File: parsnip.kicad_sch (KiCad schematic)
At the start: 68 parts, among them J1 SPI BUS, J2 I2C3, J3 I2C1, J4 I2C2, J5 e-Ink Display Connector, J6 UART0, SW1 ESP_RESET, SW2 BOOT, U1 ESP32-S3-WROOM-1-N16R8, Y1 32.768KHz

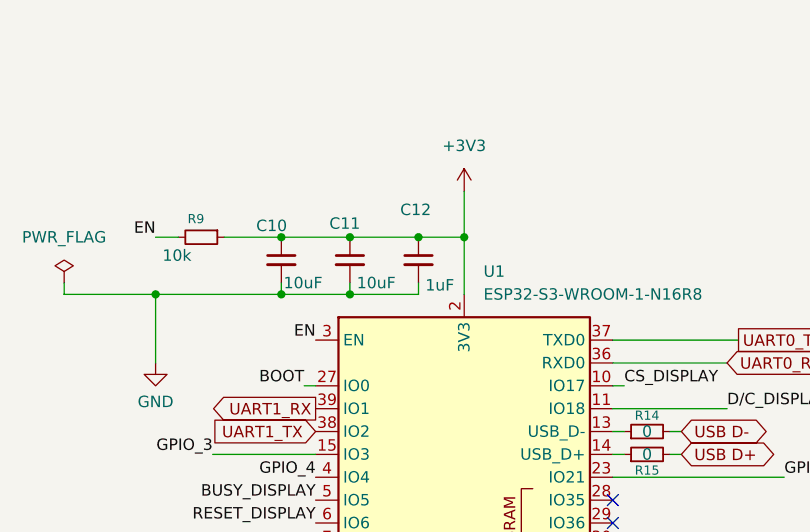
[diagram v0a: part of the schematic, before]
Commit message: change capacitor sizing & update footprints
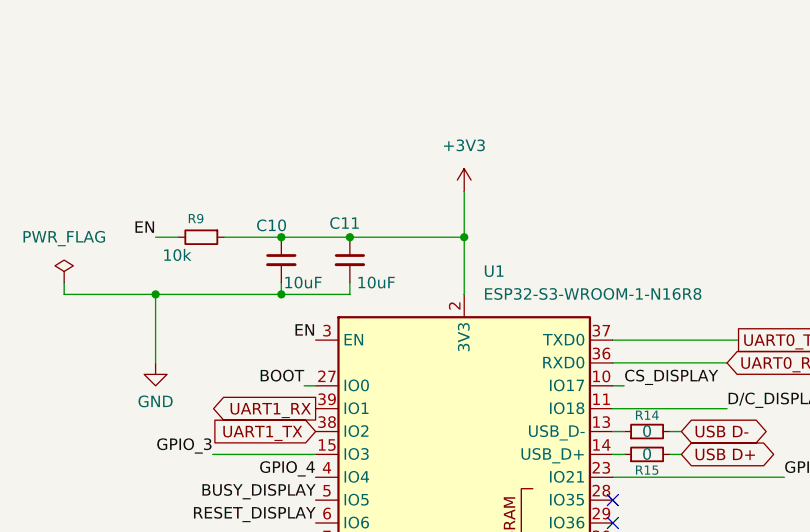
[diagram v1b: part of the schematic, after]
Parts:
- removed C12: 1uF, Capacitor_SMD:C_0402_1005Metric, symbol Device:C_Small
- SW1, SW2: LCSC Part C2681476 -> C202388
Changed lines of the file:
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@@
 	)
 	(junction
-		(at 83.82 36.83)
-		(diameter 0)
-		(color 0 0 0 0)
-	)
-	(junction
 		(at 30.48 170.18)
 		(diameter 0)
@@
 	)
 	(junction
-		(at 76.2 43.18)
-		(diameter 0)
-		(color 0 0 0 0)
-	)
-	(junction
 		(at 269.24 121.92)
 		(diameter 0)
@@
 	(wire
 		(pts
-			(xy 76.2 36.83) (xy 83.82 36.83)
+			(xy 76.2 36.83) (xy 88.9 36.83)
 		)
 		(stroke
@@
 	(wire
 		(pts
-			(xy 76.2 43.18) (xy 83.82 43.18)
-		)
-		(stroke
-			(width 0)
-			(type default)
-		)
-	)
-	(wire
-		(pts
 			(xy 236.22 49.53) (xy 248.92 49.53)
 		)
@@
 	(wire
 		(pts
-			(xy 83.82 43.18) (xy 83.82 41.91)
-		)
-		(stroke
-			(width 0)
-			(type default)
-		)
-	)
-	(wire
-		(pts
 			(xy 30.48 170.18) (xy 30.48 173.99)
 		)
@@
 	(wire
 		(pts
-			(xy 83.82 36.83) (xy 88.9 36.83)
-		)
-		(stroke
-			(width 0)
-			(type default)
-		)
-	)
-	(wire
-		(pts
 			(xy 251.46 127) (xy 256.54 127)
 		)
@@
 			)
 		)
-		(property "LCSC Part" "C2681476"
+		(property "LCSC Part" "C202388"
 			(at 177.8 29.21 0)
 			(hide yes)
@@
 	)
 	(symbol
-		(lib_id "Device:C_Small")
-		(at 83.82 39.37 0)
-		(unit 1)
-		(body_style 1)
-		(exclude_from_sim no)
-		(in_bom yes)
-		(on_board yes)
-		(in_pos_files yes)
-		(dnp no)
-		(property "Reference" "C12"
-			(at 81.788 33.782 0)
-			(show_name no)
-			(do_not_autoplace no)
-			(effects
-				(font
-					(size 1.27 1.27)
-				)
-				(justify left)
-			)
-		)
-		(property "Value" "1uF"
-			(at 84.582 42.164 0)
-			(show_name no)
-			(do_not_autoplace no)
-			(effects
-				(font
-					(size 1.27 1.27)
-				)
-				(justify left)
-			)
-		)
-		(property "Footprint" "Capacitor_SMD:C_0402_1005Metric"
-			(at 83.82 39.37 0)
-			(hide yes)
-			(show_name no)
-			(do_not_autoplace no)
-			(effects
-				(font
-					(size 1.27 1.27)
-				)
-			)
-		)
-		(property "Datasheet" ""
-			(at 83.82 39.37 0)
-			(hide yes)
-			(show_name no)
-			(do_not_autoplace no)
-			(effects
-				(font
-					(size 1.27 1.27)
-				)
-			)
-		)
-		(property "Description" "Unpolarized capacitor, small symbol"
-			(at 83.82 39.37 0)
-			(hide yes)
-			(show_name no)
-			(do_not_autoplace no)
-			(effects
-				(font
-					(size 1.27 1.27)
-				)
-			)
-		)
-		(property "LCSC Part" "C53426846"
-			(at 83.82 39.37 0)
-			(hide yes)
-			(show_name no)
-			(do_not_autoplace no)
-			(effects
-				(font
-					(size 1.27 1.27)
-				)
-			)
-		)
-		(property "Voltage Rating" "25V"
-			(at 81.026 38.862 0)
-			(hide yes)
-			(show_name no)
-			(do_not_autoplace no)
-			(effects
-				(font
-					(size 1.27 1.27)
-				)
-			)
-		)
-		(property "Tolerance" ""
-			(at 83.82 39.37 0)
-			(hide yes)
-			(show_name no)
-			(do_not_autoplace no)
-			(effects
-				(font
-					(size 1.27 1.27)
-				)
-			)
-		)
-		(property "LCSC" ""
-			(at 83.82 39.37 0)
-			(hide yes)
-			(show_name no)
-			(do_not_autoplace no)
-			(effects
-				(font
-					(size 1.27 1.27)
-				)
-			)
-		)
-		(property "KLC_S3.3" ""
-			(at 83.82 39.37 0)
-			(hide yes)
-			(show_name no)
-			(do_not_autoplace no)
-			(effects
-				(font
-					(size 1.27 1.27)
-				)
-			)
-		)
-		(property "KLC_S5.1" ""
-			(at 83.82 39.37 0)
-			(hide yes)
-			(show_name no)
-			(do_not_autoplace no)
-			(effects
-				(font
-					(size 1.27 1.27)
-				)
-			)
-		)
-		(property "Capacitor Rating" "X7R"
-			(at 83.82 39.37 0)
-			(hide yes)
-			(show_name no)
-			(do_not_autoplace no)
-			(effects
-				(font
-					(size 1.27 1.27)
-				)
-			)
-		)
-		(pin "2"
-		)
-		(pin "1"
-		)
-		(instances
-			(project "parsnip"
-				(path "/fe9d4a31-2311-442f-997c-52ad8ca5cfe9"
-					(reference "C12")
-					(unit 1)
-				)
-			)
-		)
-	)
-	(symbol
 		(lib_id "Device:R_Small")
 		(at 259.08 142.24 90)
@@
 			)
 		)
-		(property "LCSC Part" "C2681476"
+		(property "LCSC Part" "C202388"
 			(at 139.7 29.21 0)
 			(hide yes)

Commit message: assign lcsc part numbers
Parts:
- J4: now left out of the parts list
- J6: LCSC Part (none) -> C160403
- R20, R24, R25, R26, R7, R9: LCSC Part C2902636 -> C54951138
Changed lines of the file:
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@@
 		(body_style 1)
 		(exclude_from_sim no)
-		(in_bom yes)
+		(in_bom no)
 		(on_board yes)
 		(in_pos_files yes)
@@
 			)
 		)
+		(property "Capacitor Rating" ""
+			(at 113.03 177.8 0)
+			(hide yes)
+			(show_name no)
+			(do_not_autoplace no)
+			(effects
+				(font
+					(size 1.27 1.27)
+				)
+			)
+		)
 		(pin "2"
 		)
@@
 			)
 		)
-		(property "LCSC Part" "C2902636"
+		(property "LCSC Part" "C54951138"
 			(at 59.69 36.83 0)
 			(hide yes)
@@
 			)
 		)
-		(property "LCSC Part" "C2902636"
+		(property "LCSC Part" "C54951138"
 			(at 259.08 153.67 0)
 			(hide yes)
@@
 			)
 		)
-		(property "LCSC Part" "C2902636"
+		(property "LCSC Part" "C54951138"
 			(at 154.94 21.59 0)
 			(hide yes)
@@
 			)
 		)
-		(property "LCSC Part" "C2902636"
+		(property "LCSC Part" "C54951138"
 			(at 259.08 147.32 0)
 			(hide yes)
@@
 			)
 		)
-		(property "LCSC Part" "C2902636"
+		(property "LCSC Part" "C54951138"
 			(at 248.92 121.92 0)
 			(hide yes)
@@
 			)
 		)
-		(property "LCSC Part" "C2902636"
+		(property "LCSC Part" "C54951138"
 			(at 259.08 142.24 0)
 			(hide yes)
@@
 			)
 		)
-		(property "LCSC Part" ""
+		(property "LCSC Part" "C160403"
 			(at 198.12 147.32 0)
 			(hide yes)

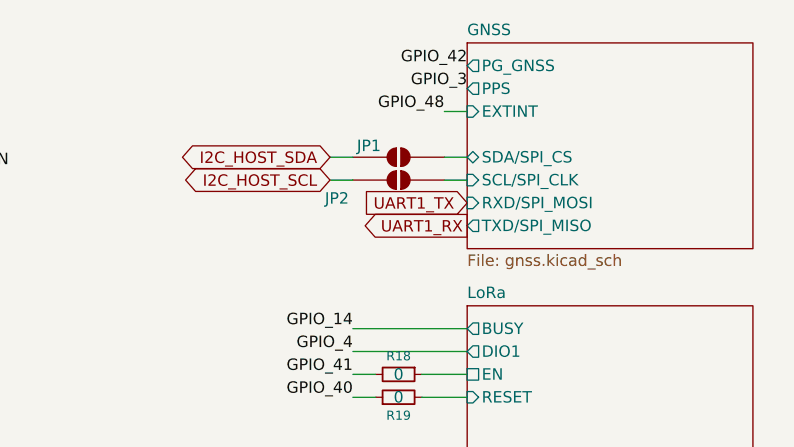
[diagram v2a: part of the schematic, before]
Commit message: Update GNSS schematic to work with NEO-F10N by changing symbol & replacing SAW filter
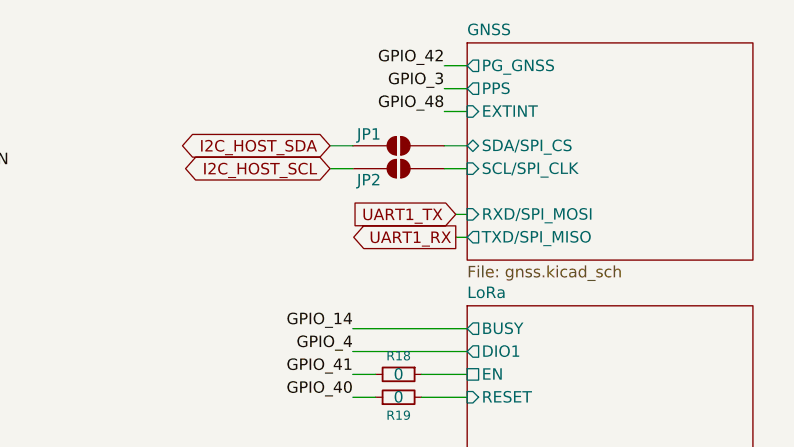
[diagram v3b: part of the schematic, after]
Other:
- moved on the sheet: JP1, JP2
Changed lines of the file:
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@@
 	(wire
 		(pts
+			(xy 246.38 17.78) (xy 248.92 17.78)
+		)
+		(stroke
+			(width 0)
+			(type default)
+		)
+	)
+	(wire
+		(pts
 			(xy 180.34 34.29) (xy 185.42 34.29)
 		)
@@
 	(wire
 		(pts
+			(xy 233.68 26.67) (xy 236.22 26.67)
+		)
+		(stroke
+			(width 0)
+			(type default)
+		)
+	)
+	(wire
+		(pts
 			(xy 62.23 104.14) (xy 62.23 97.79)
 		)
@@
 	(wire
 		(pts
-			(xy 233.68 27.94) (xy 236.22 27.94)
+			(xy 246.38 26.67) (xy 248.92 26.67)
 		)
 		(stroke
@@
 	(wire
 		(pts
+			(xy 246.38 20.32) (xy 248.92 20.32)
+		)
+		(stroke
+			(width 0)
+			(type default)
+		)
+	)
+	(wire
+		(pts
 			(xy 111.76 60.96) (xy 113.03 60.96)
 		)
@@
 	(wire
 		(pts
+			(xy 233.68 29.21) (xy 236.22 29.21)
+		)
+		(stroke
+			(width 0)
+			(type default)
+		)
+	)
+	(wire
+		(pts
 			(xy 44.45 43.18) (xy 54.61 43.18)
 		)
@@
 	(wire
 		(pts
-			(xy 22.86 170.18) (xy 30.48 170.18)
+			(xy 246.38 29.21) (xy 248.92 29.21)
 		)
 		(stroke
@@
 	(wire
 		(pts
-			(xy 142.24 176.53) (xy 138.43 176.53)
+			(xy 247.65 34.29) (xy 248.92 34.29)
 		)
 		(stroke
@@
 	(wire
 		(pts
-			(xy 246.38 27.94) (xy 248.92 27.94)
+			(xy 22.86 170.18) (xy 30.48 170.18)
+		)
+		(stroke
+			(width 0)
+			(type default)
+		)
+	)
+	(wire
+		(pts
+			(xy 142.24 176.53) (xy 138.43 176.53)
 		)
 		(stroke
@@
 	(wire
 		(pts
-			(xy 124.46 63.5) (xy 105.41 63.5)
+			(xy 247.65 36.83) (xy 248.92 36.83)
 		)
 		(stroke
@@
 	(wire
 		(pts
-			(xy 269.24 127) (xy 269.24 132.08)
+			(xy 124.46 63.5) (xy 105.41 63.5)
 		)
 		(stroke
@@
 	(wire
 		(pts
-			(xy 88.9 31.75) (xy 88.9 36.83)
+			(xy 269.24 127) (xy 269.24 132.08)
 		)
 		(stroke
@@
 	(wire
 		(pts
-			(xy 246.38 30.48) (xy 248.92 30.48)
+			(xy 88.9 31.75) (xy 88.9 36.83)
 		)
 		(stroke
@@
 	(wire
 		(pts
-			(xy 233.68 30.48) (xy 236.22 30.48)
-		)
-		(stroke
-			(width 0)
-			(type default)
-		)
-	)
-	(wire
-		(pts
 			(xy 146.05 29.21) (xy 147.32 29.21)
 		)
@@
 	)
 	(label "GPIO_42"
-		(at 248.92 17.78 180)
+		(at 246.38 17.78 180)
 		(effects
 			(font
@@
 	)
 	(label "GPIO_3"
-		(at 248.92 20.32 180)
+		(at 246.38 20.32 180)
 		(effects
 			(font
@@
 	(global_label "UART1_RX"
 		(shape output)
-		(at 248.92 35.56 180)
+		(at 247.65 36.83 180)
 		(fields_autoplaced yes)
 		(effects
@@
 		)
 		(property "Intersheetrefs" "${INTERSHEET_REFS}"
-			(at 236.6215 35.56 0)
+			(at 235.3515 36.83 0)
 			(hide yes)
 			(show_name no)
@@
 	(global_label "I2C_HOST_SCL"
 		(shape bidirectional)
-		(at 233.68 30.48 180)
+		(at 233.68 29.21 180)
 		(fields_autoplaced yes)
 		(effects
@@
 		)
 		(property "Intersheetrefs" "${INTERSHEET_REFS}"
-			(at 216.2183 30.48 0)
+			(at 216.2183 29.21 0)
 			(hide yes)
 			(show_name no)
@@
 	(global_label "I2C_HOST_SDA"
 		(shape bidirectional)
-		(at 233.68 27.94 180)
+		(at 233.68 26.67 180)
 		(fields_autoplaced yes)
 		(effects
@@
 		)
 		(property "Intersheetrefs" "${INTERSHEET_REFS}"
-			(at 216.1578 27.94 0)
+			(at 216.1578 26.67 0)
 			(hide yes)
 			(show_name no)
@@
 	(global_label "UART1_TX"
 		(shape input)
-		(at 248.92 33.02 180)
+		(at 247.65 34.29 180)
 		(fields_autoplaced yes)
 		(effects
@@
 		)
 		(property "Intersheetrefs" "${INTERSHEET_REFS}"
-			(at 236.9239 33.02 0)
+			(at 235.6539 34.29 0)
 			(hide yes)
 			(show_name no)
@@
 	(symbol
 		(lib_id "Jumper:SolderJumper_2_Open")
-		(at 241.3 30.48 0)
+		(at 241.3 29.21 0)
 		(unit 1)
 		(body_style 1)
@@
 		(dnp no)
 		(property "Reference" "JP2"
-			(at 234.442 32.512 0)
+			(at 237.998 30.48 0)
 			(show_name no)
 			(do_not_autoplace no)
@@
 		)
 		(property "Value" "SolderJumper_2_Open"
-			(at 241.3 26.67 0)
+			(at 241.3 25.4 0)
 			(hide yes)
 			(show_name no)
@@
 		)
 		(property "Footprint" "Jumper:SolderJumper-2_P1.3mm_Open_TrianglePad1.0x1.5mm"
-			(at 241.3 30.48 0)
+			(at 241.3 29.21 0)
 			(hide yes)
 			(show_name no)
@@
 		)
 		(property "Datasheet" ""
-			(at 241.3 38.1 0)
+			(at 241.3 36.83 0)
 			(hide yes)
 			(show_name no)
@@
 		)
 		(property "Description" "Solder Jumper, 2-pole, open"
-			(at 241.3 35.56 0)
+			(at 241.3 34.29 0)
 			(hide yes)
 			(show_name no)
@@
 	(symbol
 		(lib_id "Jumper:SolderJumper_2_Open")
-		(at 241.3 27.94 0)
+		(at 241.3 26.67 0)
 		(unit 1)
 		(body_style 1)
@@
 		(dnp no)
 		(property "Reference" "JP1"
-			(at 237.998 26.67 0)
+			(at 237.998 25.4 0)
 			(show_name no)
 			(do_not_autoplace no)
@@
 		)
 		(property "Value" "SolderJumper_2_Open"
-			(at 241.3 24.13 0)
+			(at 241.3 22.86 0)
 			(hide yes)
 			(show_name no)
@@
 		)
 		(property "Footprint" "Jumper:SolderJumper-2_P1.3mm_Open_TrianglePad1.0x1.5mm"
-			(at 241.3 27.94 0)
+			(at 241.3 26.67 0)
 			(hide yes)
 			(show_name no)
@@
 		)
 		(property "Datasheet" ""
-			(at 241.3 35.56 0)
+			(at 241.3 34.29 0)
 			(hide yes)
 			(show_name no)
@@
 		)
 		(property "Description" "Solder Jumper, 2-pole, open"
-			(at 241.3 33.02 0)
+			(at 241.3 31.75 0)
 			(hide yes)
 			(show_name no)
@@
 	(sheet
 		(at 248.92 15.24)
-		(size 31.75 22.86)
+		(size 31.75 24.13)
 		(exclude_from_sim no)
 		(in_bom yes)
@@
 		)
 		(property "Sheetfile" "gnss.kicad_sch"
-			(at 248.92 38.6846 0)
+			(at 248.92 39.9546 0)
 			(show_name no)
 			(do_not_autoplace no)
@@
 		)
 		(pin "RXD{slash}SPI_MOSI" input
-			(at 248.92 33.02 180)
+			(at 248.92 34.29 180)
 			(effects
 				(font
@@
 		)
 		(pin "SCL{slash}SPI_CLK" input
-			(at 248.92 30.48 180)
+			(at 248.92 29.21 180)
 			(effects
 				(font
@@
 		)
 		(pin "TXD{slash}SPI_MISO" output
-			(at 248.92 35.56 180)
+			(at 248.92 36.83 180)
 			(effects
 				(font
@@
 		)
 		(pin "SDA{slash}SPI_CS" bidirectional
-			(at 248.92 27.94 180)
+			(at 248.92 26.67 180)
 			(effects
 				(font

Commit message: backup before switching to kicad-nightly
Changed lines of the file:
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@@
 	)
 	(junction
-		(at 30.48 170.18)
+		(at 30.48 168.91)
 		(diameter 0)
 		(color 0 0 0 0)
@@
 	(wire
 		(pts
-			(xy 68.58 88.9) (xy 72.39 88.9)
+			(xy 63.5 88.9) (xy 72.39 88.9)
 		)
 		(stroke
@@
 	(wire
 		(pts
-			(xy 30.48 170.18) (xy 30.48 173.99)
+			(xy 30.48 168.91) (xy 30.48 173.99)
 		)
 		(stroke
@@
 	(wire
 		(pts
+			(xy 22.86 168.91) (xy 22.86 170.18)
+		)
+		(stroke
+			(width 0)
+			(type default)
+		)
+	)
+	(wire
+		(pts
 			(xy 30.48 179.07) (xy 31.75 179.07)
 		)
@@
 	(wire
 		(pts
-			(xy 22.86 170.18) (xy 30.48 170.18)
+			(xy 22.86 168.91) (xy 30.48 168.91)
 		)
 		(stroke
@@
 	(wire
 		(pts
-			(xy 30.48 168.91) (xy 30.48 170.18)
-		)
-		(stroke
-			(width 0)
-			(type default)
-		)
-	)
-	(wire
-		(pts
 			(xy 49.53 119.38) (xy 49.53 115.57)
 		)
@@
 	)
 	(label "GPIO_14"
-		(at 68.58 88.9 180)
+		(at 63.5 88.9 180)
 		(effects
 			(font
@@
 			)
 		)
-		(property "Description" "Generic connectable mounting pin connector, single row, 01x08, script generated (kicad-library-utils/schlib/autogen/connector/)"
+		(property "Description" "CONN HEADER SMD R/A 8POS 1.25mm"
 			(at 162.56 172.72 0)
 			(hide yes)

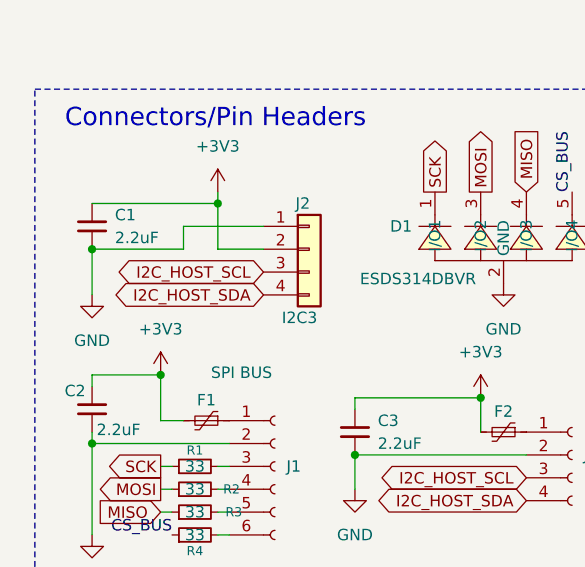
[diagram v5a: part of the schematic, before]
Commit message: swap i2c labels to follow QWIIC standard
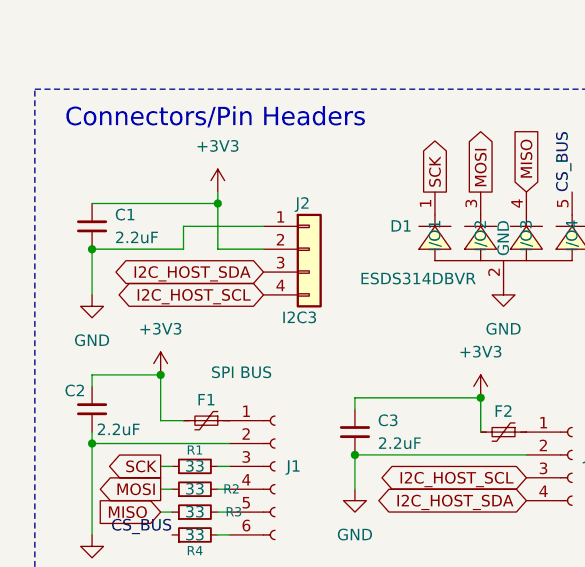
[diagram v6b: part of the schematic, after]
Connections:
- net I2C_HOST_SCL: now also J2.4 (Pin_4); no longer J2.3 (Pin_3)
- net I2C_HOST_SDA: now also J2.3 (Pin_3); no longer J2.4 (Pin_4)
